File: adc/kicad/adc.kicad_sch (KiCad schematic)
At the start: 1 part, among them U1 ADS1261IRHBR

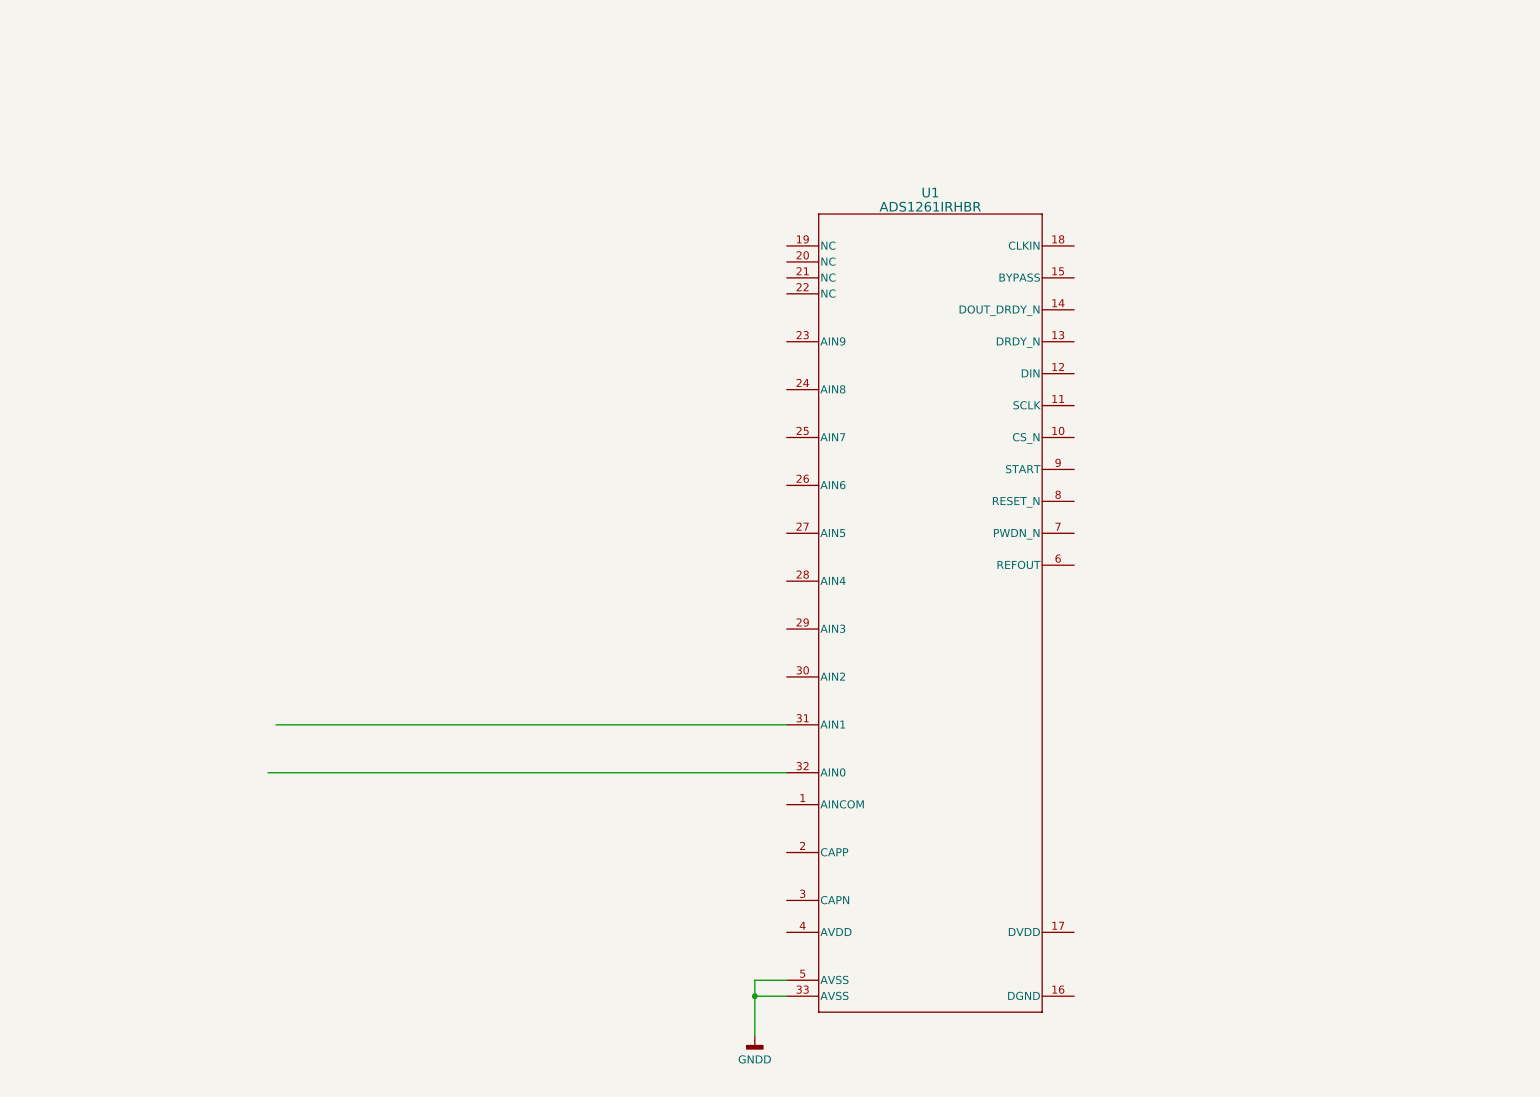
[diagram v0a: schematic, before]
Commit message: Added skeleton for 5V supply for the ADC.
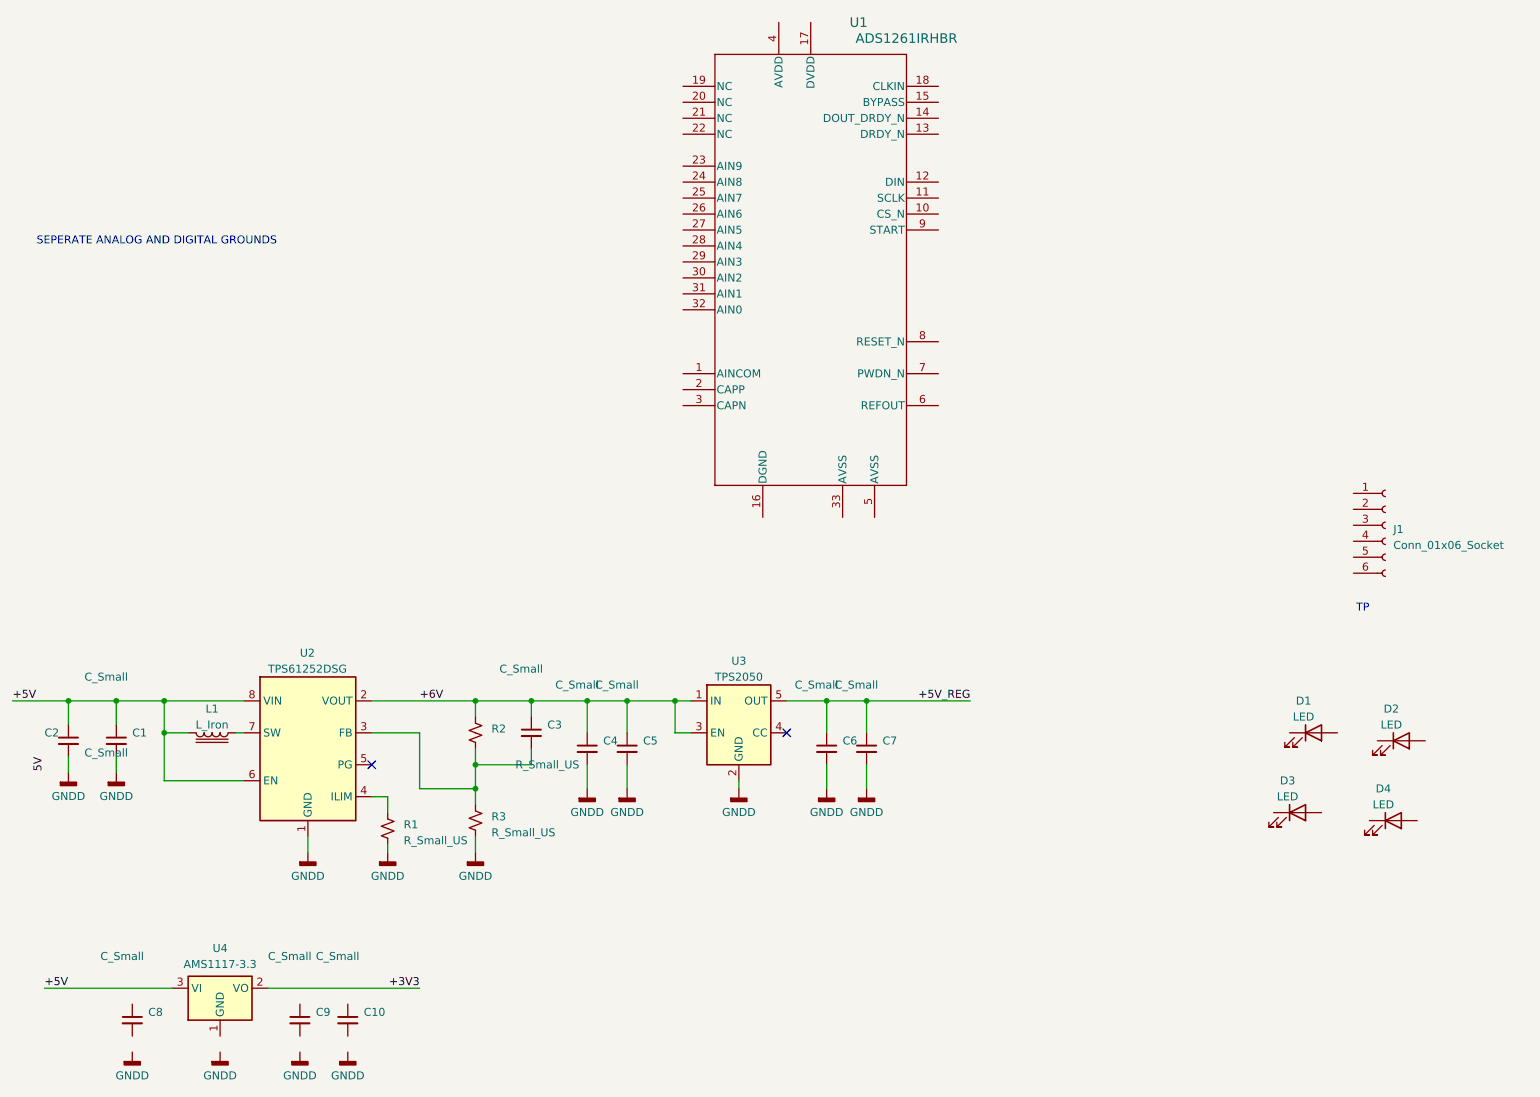
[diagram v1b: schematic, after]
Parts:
- added C1, C10, C2, C3, C4, C5, C6, C7, C8, C9: C_Small, symbol Device:C_Small
- added D1, D2, D3, D4: LED, symbol Device:LED
- added J1: Conn_01x06_Socket, symbol Connector:Conn_01x06_Socket
- added L1: L_Iron, symbol Device:L_Iron
- added R1, R2, R3: R_Small_US, symbol Device:R_Small_US
- added U2: TPS61252DSG, Package_SON:WSON-8-1EP_2x2mm_P0.5mm_EP0.9x1.6mm, symbol adc:TPS61252DSG
- added U3: TPS2050, symbol adc:TPS2050
- added U4: AMS1117-3.3, Package_TO_SOT_SMD:SOT-223-3_TabPin2, symbol Regulator_Linear:AMS1117-3.3
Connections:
- net GNDD: now also C1.2, C2.2, C4.2, C5.2, C6.2, C7.2, R1.2, R3.2, U2.1 (GND), U2.9 (GND), U3.2 (GND); no longer U1.33 (AVSS), U1.5 (AVSS)
- new net: R1.1, U2.4 (ILIM)
- new net: C3.2, R2.2, R3.1, U2.3 (FB)
- new net: L1.1, U2.7 (SW)
- new net +3V3: U4.2 (VO)
- new net +5V: C1.1, C2.1, L1.2, U2.6 (EN), U2.8 (VIN), U4.3 (VI)
- new net +5V_REG: C6.1, C7.1, U3.5 (OUT)
- new net +6V: C3.1, C4.1, C5.1, R2.1, U2.2 (VOUT), U3.1 (IN), U3.3 (EN)
- no-connect marks 0 -> 2
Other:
- note added: "SEPERATE ANALOG AND DIGITAL GROUNDS"
- note added: "TP"
- moved on the sheet: U1

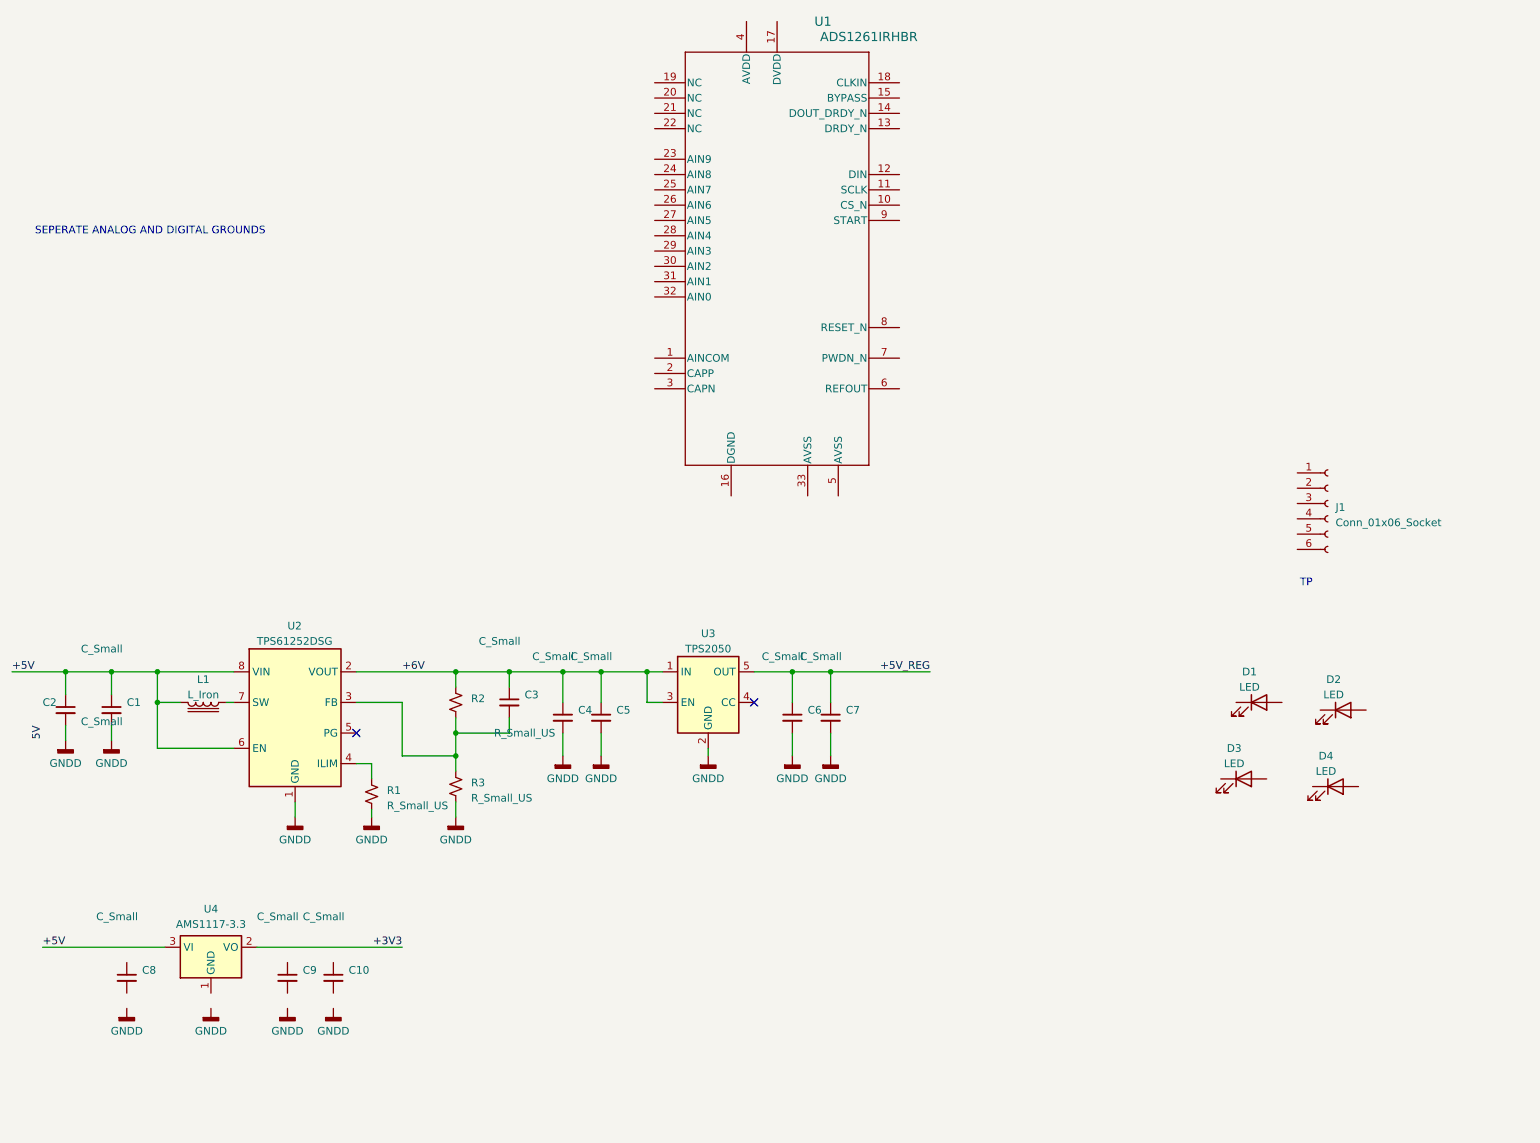
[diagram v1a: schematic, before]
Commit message: Created initial ADC card Kicad project using the breakout project.
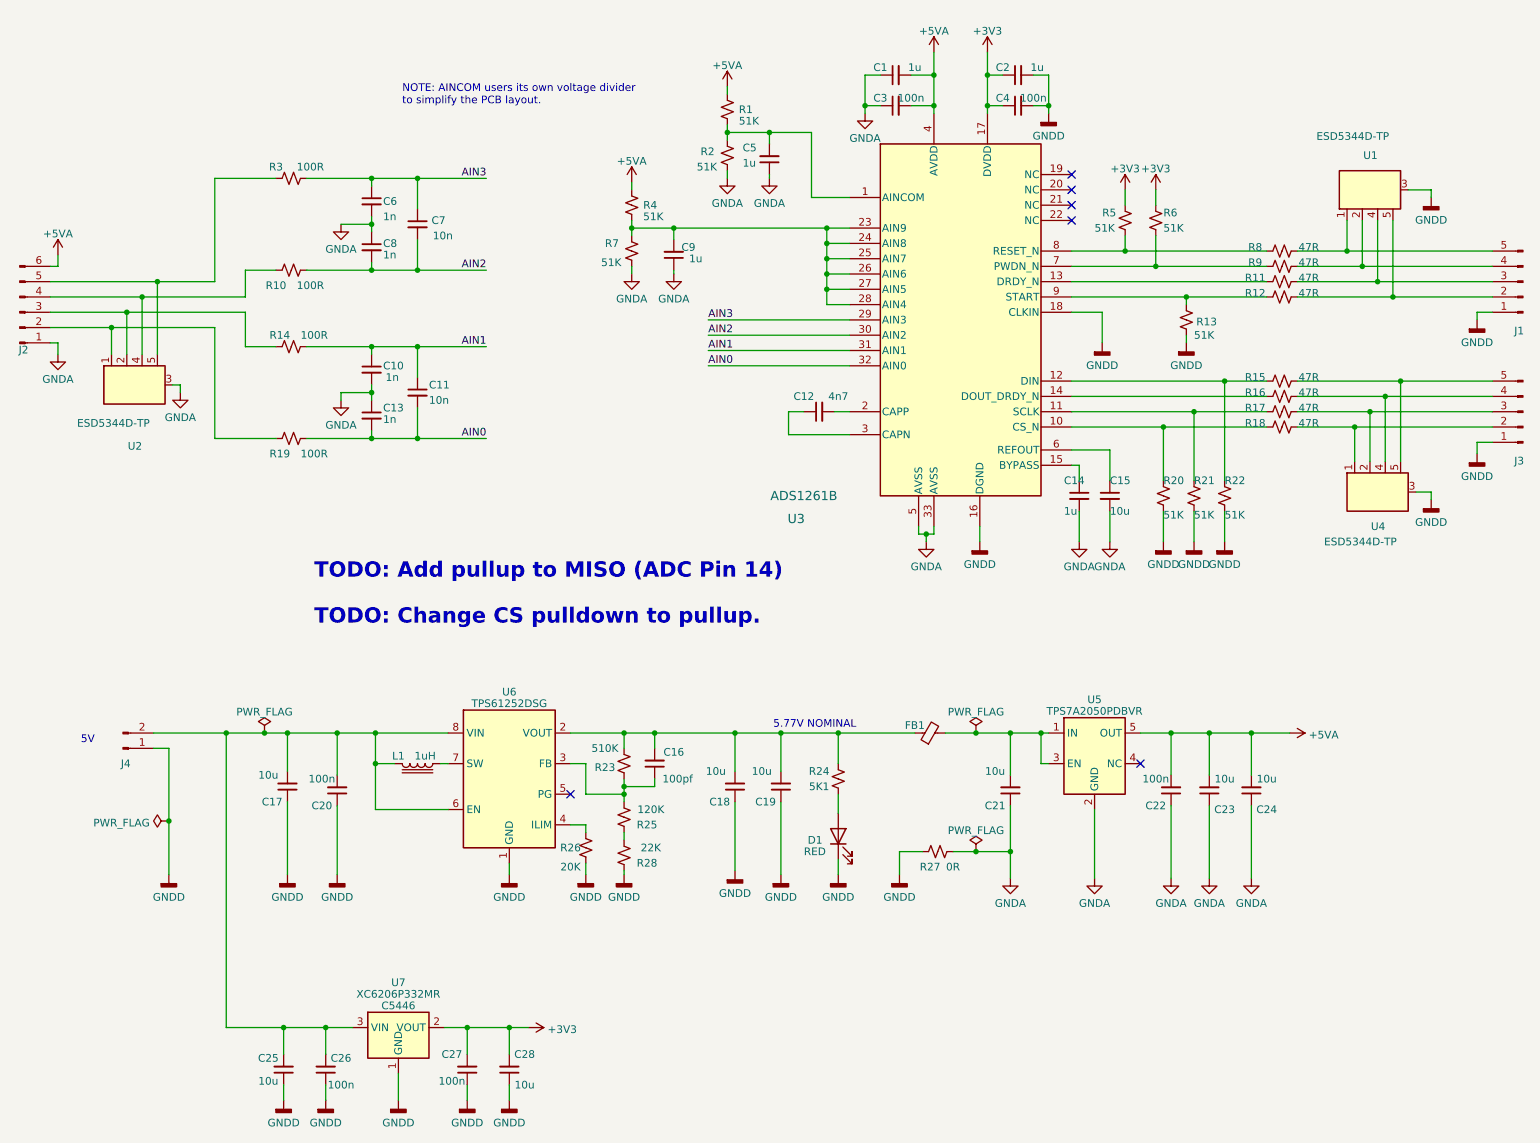
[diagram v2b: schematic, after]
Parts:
- removed D2, D3, D4: LED, symbol Device:LED
- removed J1: Conn_01x06_Socket, symbol Connector:Conn_01x06_Socket
- removed U2: TPS61252DSG, Package_SON:WSON-8-1EP_2x2mm_P0.5mm_EP0.9x1.6mm, symbol adc:TPS61252DSG
- removed U3: TPS2050, symbol adc:TPS2050
- removed U4: AMS1117-3.3, Package_TO_SOT_SMD:SOT-223-3_TabPin2, symbol Regulator_Linear:AMS1117-3.3
- added C11: 10n, Capacitor_SMD:C_0402_1005Metric, symbol Device:C_Small
- added C12: 4n7, Capacitor_SMD:C_0402_1005Metric, symbol Device:C_Small
- added C13: 1n, Capacitor_SMD:C_0402_1005Metric, symbol Device:C_Small
- added C14: 1u, Capacitor_SMD:C_0402_1005Metric, symbol Device:C_Small
- added C15, C17, C18, C19, C21, C23, C24, C25, C28: 10u, Capacitor_SMD:C_0603_1608Metric, symbol Device:C_Small
- added C16: 100pf, Capacitor_SMD:C_0402_1005Metric, symbol Device:C_Small
- added C20, C22, C26, C27: 100n, Capacitor_SMD:C_0402_1005Metric, symbol Device:C_Small
- added FB1: Ferrite Bead, Inductor_SMD:L_0805_2012Metric, symbol Device:FerriteBead_Small
- added J1, J3: Conn_01x05_Pin, adc:PinHeader_1x05_P2.54mm_Vertical, symbol Connector:Conn_01x05_Pin
- added J2: Conn_01x06_Pin, adc:PinHeader_1x06_P2.54mm_Vertical, symbol Connector:Conn_01x06_Pin
- added J4: Conn_01x03_Pin, adc:PinHeader_1x02_P2.54mm_Vertical, symbol Connector:Conn_01x02_Pin
- added R10, R14, R19: 100R, Resistor_SMD:R_0402_1005Metric, symbol Device:R_Small_US
- added R11, R12, R15, R16, R17, R18, R8, R9: 47R, Resistor_SMD:R_0402_1005Metric, symbol Device:R_Small_US
- added R13, R20, R21, R22, R4, R5, R6, R7: 51K, Resistor_SMD:R_0402_1005Metric, symbol Device:R_Small_US
- added R23: 510K, Resistor_SMD:R_0402_1005Metric, symbol Device:R_Small_US
- added R24: 5K1, Resistor_SMD:R_0402_1005Metric, symbol Device:R_Small_US
- added R25: 120K, Resistor_SMD:R_0402_1005Metric, symbol Device:R_Small_US
- added R26: 20K, Resistor_SMD:R_0402_1005Metric, symbol Device:R_Small_US
- added R27: 0R, Resistor_SMD:R_0805_2012Metric, symbol Device:R_Small_US
- added R28: 22K, Resistor_SMD:R_0402_1005Metric, symbol Device:R_Small_US
- added U1, U2, U4: ESD5344D-TP, common:Diodes_UDFN-10_1.0x2.5mm_P0.5mm, symbol common:ESD5344D
- added U5: TPS7A2050PDBVR, adc:SOT-23-5, symbol adc:TPS7A2050
- added U6: TPS61252DSG, adc:WSON-8-1EP_2x2mm_P0.5mm_EP0.9x1.6mm, symbol adc:TPS61252DSG
- added U7: XC6206P332MR, Package_TO_SOT_SMD:SOT-23-3, symbol ble:HT75xx-1-SOT89
- C1, C2, C5, C9: value C_Small -> 1u; footprint (none) -> Capacitor_SMD:C_0402_1005Metric; LCSC (none) -> C52923
- C10, C6, C8: value C_Small -> 1n; footprint (none) -> Capacitor_SMD:C_0402_1005Metric; LCSC (none) -> C1523
- C3, C4: value C_Small -> 100n; footprint (none) -> Capacitor_SMD:C_0402_1005Metric; LCSC (none) -> C1525
- C7: value C_Small -> 10n; footprint (none) -> Capacitor_SMD:C_0402_1005Metric; LCSC (none) -> C15195
- D1: value LED -> RED; footprint (none) -> LED_SMD:LED_0805_2012Metric; LCSC (none) -> C84256
- L1: value L_Iron -> 1uH; footprint (none) -> Inductor_SMD:L_1210_3225Metric; LCSC (none) -> C703782
- R1, R2: value R_Small_US -> 51K; footprint (none) -> Resistor_SMD:R_0402_1005Metric; LCSC (none) -> C25794
- R3: value R_Small_US -> 100R; footprint (none) -> Resistor_SMD:R_0402_1005Metric; LCSC (none) -> C25076
- U3: renamed from U1; value ADS1261IRHBR -> ADS1261B; footprint RHB0032E -> adc:RHB0032E; LCSC (none) -> DNP
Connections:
- net +5V_REG is gone; now on net AIN3: C6.1, C7.1
- net +3V3: now also C2.1, C4.1, U3.17 (DVDD), C27.2, C28.2, R5.2, R6.2, U7.2 (VOUT)
- net GNDD: now also D1.1 (K), U3.16 (DGND), U3.18 (CLKIN), C17.1, C18.1, C19.1, C20.1, C25.1, C26.1, C27.1, C28.1, J1.1 (Pin_1), J3.1 (Pin_1), J4.1 (Pin_1), R13.1, R20.1, R21.1, R22.1, R26.2, R27.1, R28.1, U1.3 (GND), U4.3 (GND), U6.1 (GND), U6.9 (GND), U7.1 (GND); no longer C1.2, C5.2, C6.2, C7.2, R1.2, R3.2
- net AIN1: now reaches C10.1
- net AIN1: now also U3.31 (AIN1), C11.1, R14.2
- net GNDA: now reaches C10.2
- net GNDA: now also C1.1, C3.1, C5.1, C6.2, C8.1, C9.1, R2.1, U3.33 (AVSS), U3.5 (AVSS), C13.1, C14.2, C15.2, C21.1, C22.1, C23.1, C24.1, J2.1 (Pin_1), R27.2, R7.1, U2.3 (GND), U5.2 (GND)
- net at D1.2 (A): now also R24.2
- net at R1.1: now also C5.2, R2.2, U3.1 (AINCOM)
- net at U3.10 (CS_N): now also R18.2, R20.2
- net at U3.11 (SCLK): now also R17.2, R21.2
- net at U3.12 (DIN): now also R15.2, R22.2
- net at U3.13 (DRDY_N): now also R11.2
- net at U3.14 (DOUT_DRDY_N): now also R16.2
- net at U3.15 (BYPASS): now also C14.1
- net at U3.2 (CAPP): now also C12.2
- net at U3.23 (AIN9): now also C9.2, U3.24 (AIN8), U3.25 (AIN7), U3.26 (AIN6), U3.27 (AIN5), U3.28 (AIN4), R4.1, R7.2
- net AIN3: now reaches U3.29 (AIN3)
- net AIN3: now also R3.2
- net at U3.3 (CAPN): now also C12.1
- net AIN2: now reaches U3.30 (AIN2)
- net AIN2: now also C7.2, C8.2, R10.2
- net AIN0: now reaches U3.32 (AIN0)
- net AIN0: now also C11.2, C13.2, R19.2
- net +5VA: now reaches U3.4 (AVDD)
- net +5VA: now also C1.2, C3.2, R1.2, C22.2, C23.2, C24.2, J2.6 (Pin_6), R4.2, U5.5 (OUT)
- net at U3.6 (REFOUT): now also C15.1
- net at U3.7 (PWDN_N): now also R6.1, R9.2
- net at U3.8 (RESET_N): now also R5.1, R8.2
- net at U3.9 (START): now also R12.2, R13.2
- net at L1.1: now also C17.2, C20.2, C25.2, C26.2, J4.2 (Pin_2), U6.6 (EN), U6.8 (VIN), U7.3 (VIN)
- removed net +5V: C1.1, C2.1, L1.2
- removed net +6V: C3.1, C4.1, C5.1, R2.1
- new net: C21.2, FB1.2, U5.1 (IN), U5.3 (EN)
- new net: J2.2 (Pin_2), R19.1, U2.1 (D1)
- new net: J1.2 (Pin_2), R12.1, U1.5 (D4)
- new net: J3.2 (Pin_2), R18.1, U4.1 (D1)
- new net: J3.3 (Pin_3), R17.1, U4.2 (D2)
- new net: J3.4 (Pin_4), R16.1, U4.4 (D3)
- new net: J3.5 (Pin_5), R15.1, U4.5 (D4)
- new net: J2.4 (Pin_4), R10.1, U2.4 (D3)
- new net: J1.3 (Pin_3), R11.1, U1.4 (D3)
- new net: C16.2, C18.2, C19.2, FB1.1, R23.1, R24.1, U6.2 (VOUT)
- new net: C16.1, R23.2, R25.2, U6.3 (FB)
- new net: J2.3 (Pin_3), R14.1, U2.2 (D2)
- new net: R26.1, U6.4 (ILIM)
- new net: L1.2, U6.7 (SW)
- new net: R25.1, R28.2
- new net: J1.4 (Pin_4), R9.1, U1.2 (D2)
- new net: J2.5 (Pin_5), R3.1, U2.5 (D4)
- new net: J1.5 (Pin_5), R8.1, U1.1 (D1)
- no-connect marks 2 -> 6
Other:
- note added: "5.77V NOMINAL"
- note added: "5V"
- note added: "NOTE: AINCOM users its own voltage divider to simplify the PCB layout."
- note added: "TODO: Add pullup to MISO (ADC Pin 14)"
- note added: "TODO: Change CS pulldown to pullup."
- note removed: "SEPERATE ANALOG AND DIGITAL GROUNDS"
- note removed: "TP"
- title: (none) -> ADS1261 ADC BOARD
